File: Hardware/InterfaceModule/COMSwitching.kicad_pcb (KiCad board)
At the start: 2 copper layers, 76 x 76 mm, 15 parts, among them J15 D-700 COM, J16 TS-480 COM, J17 External COM, K15 FINDER-40.52, K16 FINDER-40.52, K17 FINDER-40.52, K18 FINDER-40.52, K19 FINDER-40.52, K20 FINDER-40.52, K21 FINDER-40.52, K22 FINDER-40.52

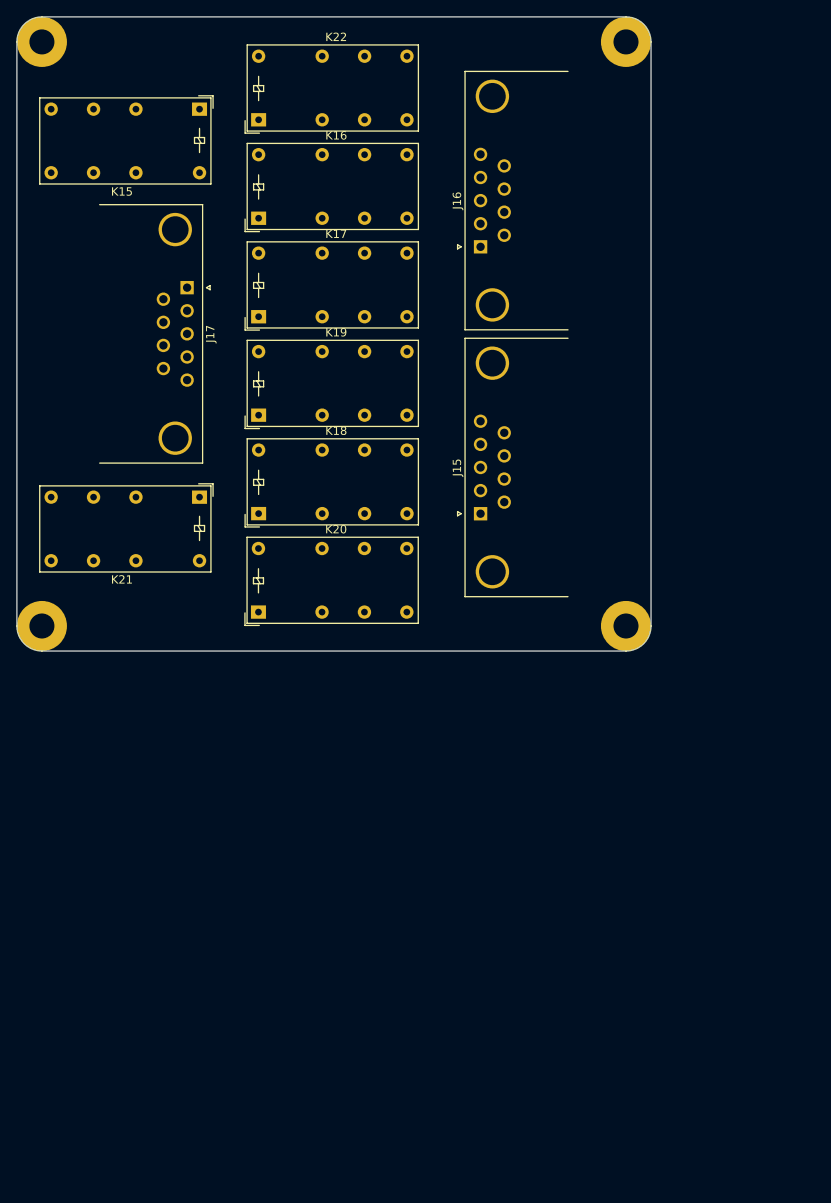
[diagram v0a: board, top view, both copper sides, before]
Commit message: Updated silkscreen dates, corrected gerber files
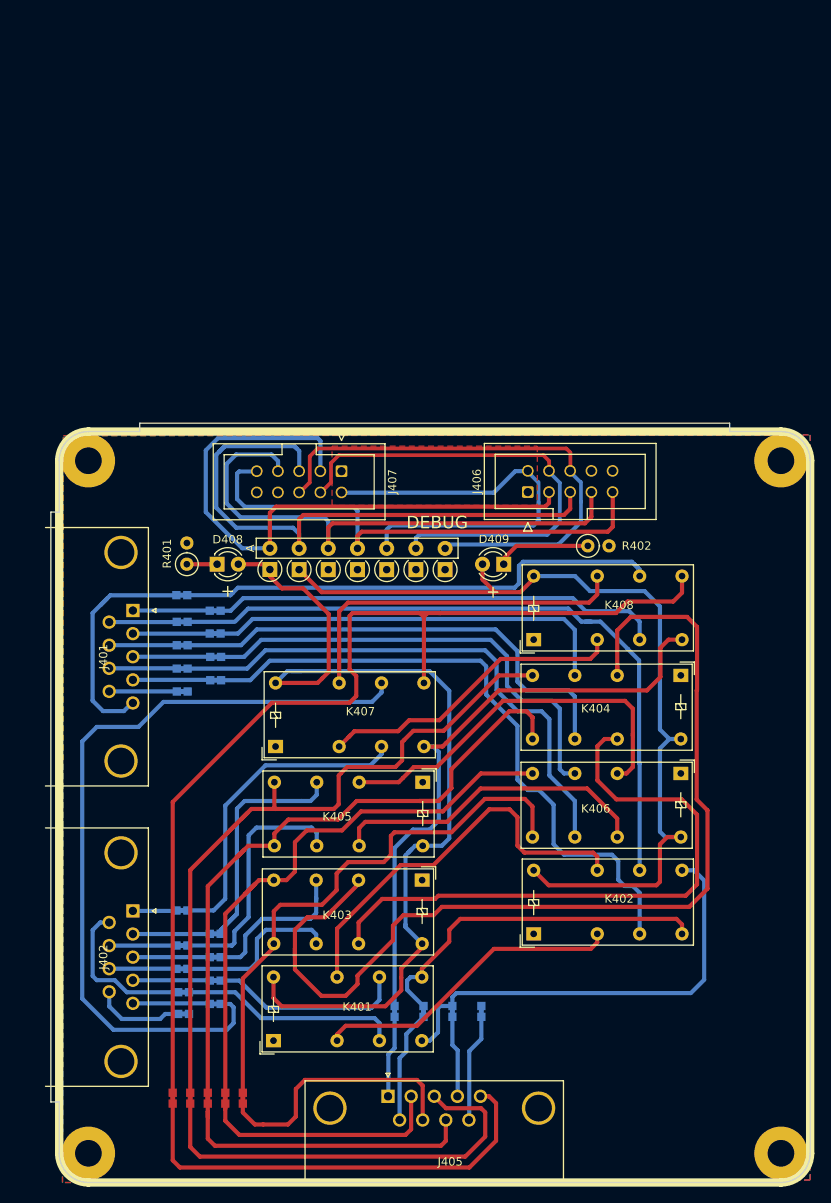
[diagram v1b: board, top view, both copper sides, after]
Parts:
- removed H1, H2, H3, H4: MountingHole_Pad, 
- removed J15: D-700 COM, Connector_Dsub:DSUB-9_Male_Horizontal_P2.77x2.84mm_EdgePinOffset7.70mm_Housed_MountingHolesOffset9.12mm
- removed J16: TS-480 COM, Connector_Dsub:DSUB-9_Male_Horizontal_P2.77x2.84mm_EdgePinOffset7.70mm_Housed_MountingHolesOffset9.12mm
- removed J17: External COM, Connector_Dsub:DSUB-9_Male_Horizontal_P2.77x2.84mm_EdgePinOffset7.70mm_Housed_MountingHolesOffset9.12mm
- removed K15, K16, K17, K18, K19, K20, K21, K22: FINDER-40.52, Relay_THT:Relay_DPDT_Finder_30.22
- added D401: D_Small_Filled, Diode_THT:D_A-405_P2.54mm_Vertical_AnodeUp, F.Cu at (132.8, 124.0)
- added D402: D_Small_Filled, Diode_THT:D_A-405_P2.54mm_Vertical_AnodeUp, F.Cu at (136.3, 124.0)
- added D403: D_Small_Filled, Diode_THT:D_A-405_P2.54mm_Vertical_AnodeUp, F.Cu at (139.8, 124.0)
- added D404: D_Small_Filled, Diode_THT:D_A-405_P2.54mm_Vertical_AnodeUp, F.Cu at (143.3, 124.0)
- added D405: D_Small_Filled, Diode_THT:D_A-405_P2.54mm_Vertical_AnodeUp, F.Cu at (146.8, 124.0)
- added D406: D_Small_Filled, Diode_THT:D_A-405_P2.54mm_Vertical_AnodeUp, F.Cu at (150.3, 124.0)
- added D407: D_Small_Filled, Diode_THT:D_A-405_P2.54mm_Vertical_AnodeUp, F.Cu at (153.8, 124.0)
- added D408: LED, LED_THT:LED_D3.0mm, F.Cu at (126.4, 123.4)
- added D409: LED, LED_THT:LED_D3.0mm, F.Cu at (160.8, 123.4)
- added G***: LOGO, libraries:LogoSmallInvert, B.Cu at (180.5, 190.0)
- added H401: Mounting Hole, libraries:M3_Mounting, F.Cu at (194.0, 194.0)
- added H402: Mounting Hole, libraries:M3_Mounting, F.Cu at (111.0, 111.0)
- added H403: Mounting Hole, libraries:M3_Mounting, F.Cu at (111.0, 194.0)
- added H404: Mounting Hole, libraries:M3_Mounting, F.Cu at (194.0, 111.0)
- added J401: D-700 COM, Connector_Dsub:DSUB-9_Male_Horizontal_P2.77x2.84mm_EdgePinOffset7.70mm_Housed_MountingHolesOffset9.12mm, F.Cu at (116.3, 128.9)
- added J402: TS-480 COM, Connector_Dsub:DSUB-9_Male_Horizontal_P2.77x2.84mm_EdgePinOffset7.70mm_Housed_MountingHolesOffset9.12mm, F.Cu at (116.3, 164.9)
- added J405: External COM, Connector_Dsub:DSUB-9_Male_Horizontal_P2.77x2.84mm_EdgePinOffset7.70mm_Housed_MountingHolesOffset9.12mm, F.Cu at (146.9, 187.2)
- added J406: 2x05 IDC Header - IN, Connector_IDC:IDC-Header_2x05_P2.54mm_Vertical, F.Cu at (163.7, 114.8)
- added J407: 2x05 IDC Header - OUT, Connector_IDC:IDC-Header_2x05_P2.54mm_Vertical, F.Cu at (141.3, 112.3)
- added JP401: Jumper_2_Bridged, libraries:1.0mm_Bridge, B.Cu at (126.2, 129.0)
- added JP402: Jumper_2_Bridged, libraries:1.0mm_Bridge, B.Cu at (122.2, 130.3)
- added JP403: Jumper_2_Bridged, libraries:1.0mm_Bridge, B.Cu at (126.2, 131.7)
- added JP404: Jumper_2_Bridged, libraries:1.0mm_Bridge, B.Cu at (122.2, 133.1)
- added JP405: Jumper_2_Bridged, libraries:1.0mm_Bridge, B.Cu at (126.3, 134.5)
- added JP406: Jumper_2_Bridged, libraries:1.0mm_Bridge, B.Cu at (122.2, 135.9)
- added JP407: Jumper_2_Bridged, libraries:1.0mm_Bridge, B.Cu at (126.3, 137.3)
- added JP408: Jumper_2_Bridged, libraries:1.0mm_Bridge, B.Cu at (122.3, 138.7)
- added JP409: Jumper_2_Bridged, libraries:1.0mm_Bridge, B.Cu at (122.2, 127.1)
- added JP410: Jumper_2_Bridged, libraries:1.0mm_Bridge, B.Cu at (122.2, 164.9)
- added JP411: Jumper_2_Bridged, libraries:1.0mm_Bridge, B.Cu at (122.4, 174.7)
- added JP412: Jumper_2_Bridged, libraries:1.0mm_Bridge, B.Cu at (126.2, 167.7)
- added JP413: Jumper_2_Bridged, libraries:1.0mm_Bridge, B.Cu at (122.2, 169.1)
- added JP414: Jumper_2_Bridged, libraries:1.0mm_Bridge, B.Cu at (126.2, 170.5)
- added JP415: Jumper_2_Bridged, libraries:1.0mm_Bridge, B.Cu at (122.2, 171.9)
- added JP416: Jumper_2_Bridged, libraries:1.0mm_Bridge, B.Cu at (126.2, 173.3)
- added JP417: Jumper_2_Bridged, libraries:1.0mm_Bridge, B.Cu at (122.4, 177.3)
- added JP418: Jumper_2_Bridged, libraries:1.0mm_Bridge, B.Cu at (126.2, 176.1)
- added JP419: Jumper_2_Bridged, libraries:1.0mm_Bridge, B.Cu at (147.7, 177.0)
- added JP420: Jumper_2_Bridged, libraries:1.0mm_Bridge, B.Cu at (151.2, 177.0)
- added JP421: Jumper_2_Bridged, libraries:1.0mm_Bridge, F.Cu at (127.4, 187.4)
- added JP422: Jumper_2_Bridged, libraries:1.0mm_Bridge, F.Cu at (129.5, 187.4)
- added JP423: Jumper_2_Bridged, libraries:1.0mm_Bridge, F.Cu at (123.2, 187.4)
- added JP424: Jumper_2_Bridged, libraries:1.0mm_Bridge, F.Cu at (125.3, 187.4)
- added JP425: Jumper_2_Bridged, libraries:1.0mm_Bridge, B.Cu at (154.6, 177.0)
- added JP426: Jumper_2_Bridged, libraries:1.0mm_Bridge, B.Cu at (158.1, 177.0)
- added JP427: Jumper_2_Bridged, libraries:1.0mm_Bridge, F.Cu at (121.1, 187.4)
- added K401: FINDER-40.52, Relay_THT:Relay_DPDT_Finder_30.22, F.Cu at (133.2, 180.5)
- added K402: FINDER-40.52, Relay_THT:Relay_DPDT_Finder_30.22, F.Cu at (164.4, 167.7)
- added K403: FINDER-40.52, Relay_THT:Relay_DPDT_Finder_30.22, F.Cu at (151.0, 161.3)
- added K404: FINDER-40.52, Relay_THT:Relay_DPDT_Finder_30.22, F.Cu at (182.0, 136.7)
- added K405: FINDER-40.52, Relay_THT:Relay_DPDT_Finder_30.22, F.Cu at (151.1, 149.5)
- added K406: FINDER-40.52, Relay_THT:Relay_DPDT_Finder_30.22, F.Cu at (182.0, 148.5)
- added K407: FINDER-40.52, Relay_THT:Relay_DPDT_Finder_30.22, F.Cu at (133.4, 145.2)
- added K408: FINDER-40.52, Relay_THT:Relay_DPDT_Finder_30.22, F.Cu at (164.4, 132.4)
- added R401: 680Ω, Resistor_THT:R_Axial_DIN0207_L6.3mm_D2.5mm_P2.54mm_Vertical, F.Cu at (122.8, 123.4)
- added R402: 680Ω, Resistor_THT:R_Axial_DIN0207_L6.3mm_D2.5mm_P2.54mm_Vertical, F.Cu at (170.9, 121.2)
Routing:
- net /COM Port Switching/EXT_GND: track 0.00 -> 125.6 mm
- net Net-(K403-Pad11): track 0.00 -> 122.5 mm
- net /COM Port Switching/Knob_Pos_1: track 0.00 -> 111.7 mm
- net /COM Port Switching/Knob_Pos_2: track 0.00 -> 106.3 mm
- net /COM Port Switching/480_GND: track 0.00 -> 93.2 mm
- net /COM Port Switching/EXT_TX: track 0.00 -> 86.3 mm
- net /COM Port Switching/D700_DSR: track 0.00 -> 83.1 mm
- net /COM Port Switching/EXT_CTS: track 0.00 -> 81.8 mm
- net /COM Port Switching/D700_DTR: track 0.00 -> 77.4 mm
- net /COM Port Switching/Knob_Pos_1_Raw: track 0.00 -> 74.5 mm
- net Net-(K403-Pad21): track 0.00 -> 74.3 mm
- net /COM Port Switching/EXT_NC1: track 0.00 -> 74.2 mm
- net /COM Port Switching/Knob_Pos_2_Raw: track 0.00 -> 72.1 mm
- net /COM Port Switching/EXT_RX: track 0.00 -> 69.0 mm
- net /COM Port Switching/Knob_Pos_3_Raw: track 0.00 -> 66.8 mm
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- added copper zone on F.Cu, net +12P
- added copper zone on B.Cu, net GND
- added copper zone on F.Cu, net GND
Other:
- board size 76 x 76 mm -> 91 x 91 mm
- board text added: "+"
- board text added: "COM Module Rev 1. Thomas Francois Feb 27th, 2023"
- board text added: "D-700 COM"
- board text added: "DEBUG"
- board text added: "External COM"
- board text added: "IN"
- board text added: "OUT"
- board text added: "TS-480 COM"
